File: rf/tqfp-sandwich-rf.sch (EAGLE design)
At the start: 98 parts, among them IC1 PCA9555PW, IC2 MCP6002, K0 G6KU-2G-Y-TR_DC5, K1 G6KU-2G-Y-TR_DC5, K2 G6KU-2G-Y-TR_DC5, K3 G6KU-2G-Y-TR_DC5, K4 G6KU-2G-Y-TR_DC5, Q1 MMBF170, Q2 MMBF170, Q3 MMBF170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

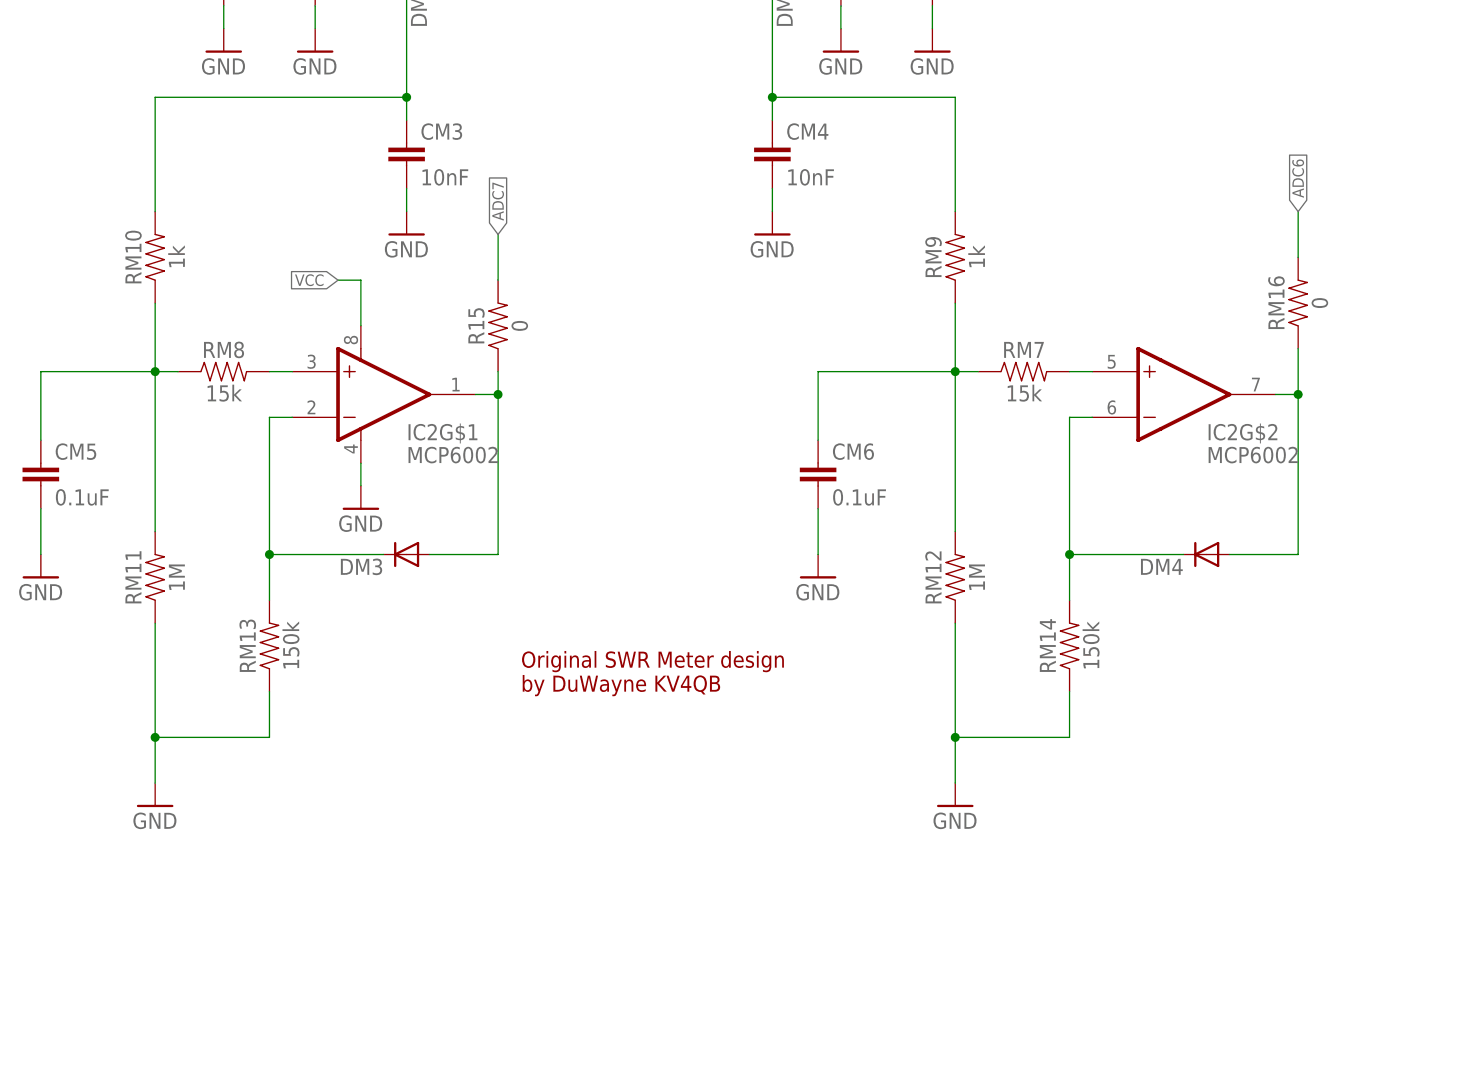
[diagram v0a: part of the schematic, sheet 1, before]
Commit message: Add capacitor on the MCP6002 power rail
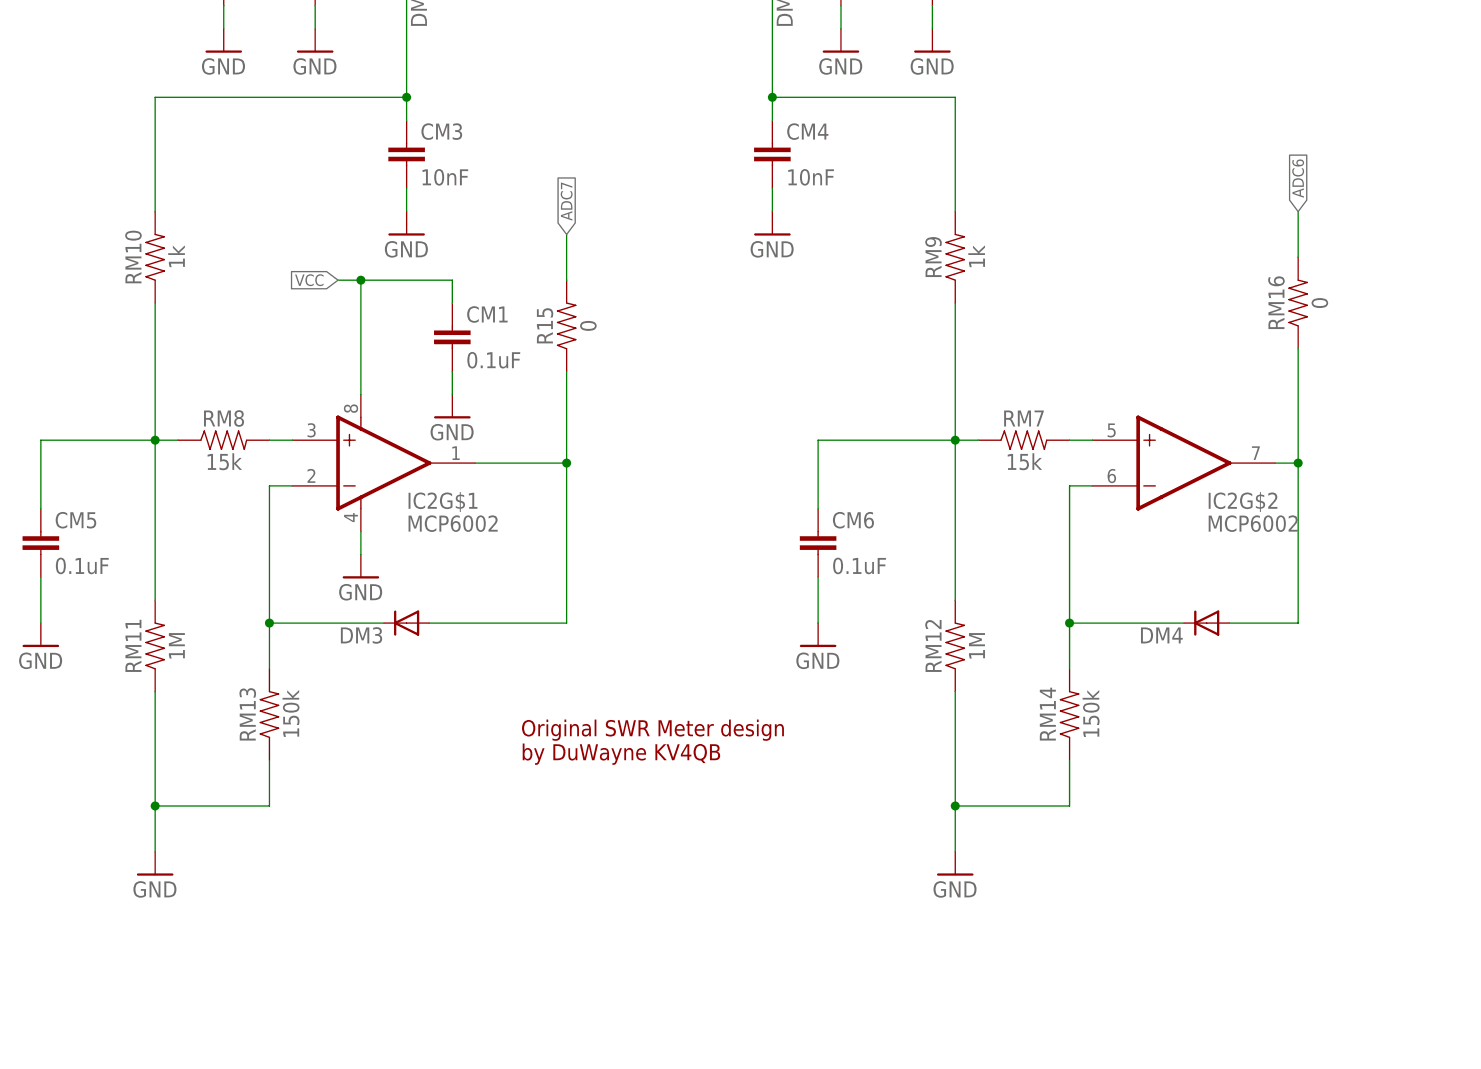
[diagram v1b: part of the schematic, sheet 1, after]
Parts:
- added CM1: 0.1uF, SparkFun-Capacitors:0.1UF-0603-100V-10%
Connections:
- net GND: now also CM1.2
- net VCC: now also CM1.1
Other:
- moved on the sheet: CM5, CM6, DM3, DM4, IC2G$1, IC2G$2, R15, RM11, RM12, RM13, RM14, RM7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

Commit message: Remove mosfets, inductors, capacitors  values.
The board can accept two different kind of finals (MMBF170 or IRLML2060).
Capacitors and inductors need to follow this choice therefore they
probably shouldn't be explicitly indicated on the schematic.
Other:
- note added: "PLEASE REFER TO ORIGINAL RF BOARDS SCHEMATICS TO FIND MMBF170 or IRLML2060 TOROIDS/CAPACITORS VALUES"
- moved on the sheet: C1, C11, C121, C122, C13, C14, C15, C2, C3, C4, C5, C80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
